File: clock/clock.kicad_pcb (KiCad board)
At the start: 2 copper layers, 176.8 x 81.3 mm, 288 parts, among them P101 CONN_01X03, P102 CONN_FAN_PWM, P103 XG4A-1631, P301 MCRF, Q201 MMBT3904, U201 PCA9306, U202 DAC8830, U203 LMV722, U204 LTC2990, U205 LP3853, U207 NC7SZ125, U301 Adafruit746, U302 MIC5225, U303 PA6H, U401 74LVC541, U501 TPS56428, U502 TPS56428, U503 TPS56428, U601 ADT7410, U602 DS3231, U603 ADT7410, Y202 CX210

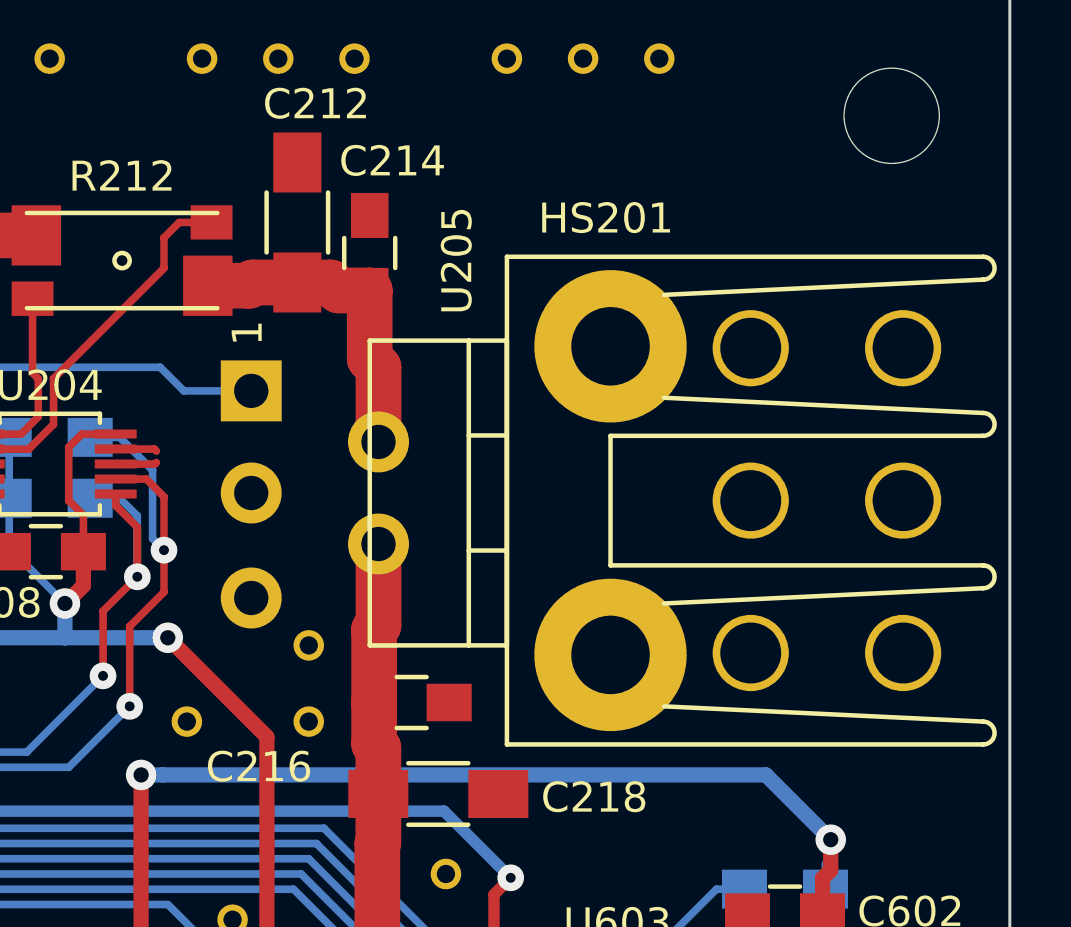
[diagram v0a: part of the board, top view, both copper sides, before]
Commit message: Fix pin location on to-220 and heatsink location. Add 7-segment display 3D model to board.
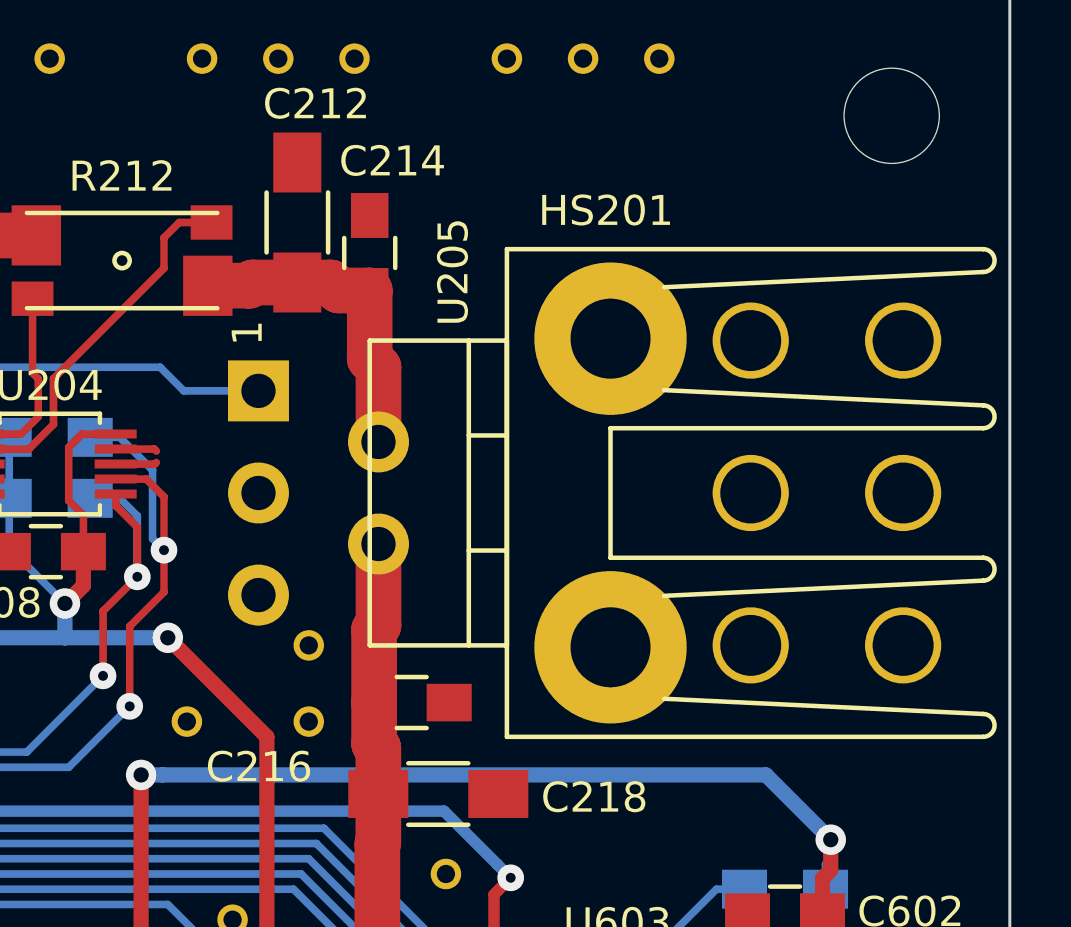
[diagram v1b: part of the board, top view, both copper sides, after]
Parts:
- moved HS201 0.25 mm to (350.5, 181.6)
- moved REF** 0.25 mm to (358.6, 186.7)
- moved REF** 0.25 mm to (363.7, 186.7)
- moved REF** 0.25 mm to (363.7, 176.5)
- moved REF** 0.25 mm to (363.7, 181.6)
- moved REF** 0.25 mm to (358.6, 176.5)
- moved REF** 0.25 mm to (358.6, 181.6)

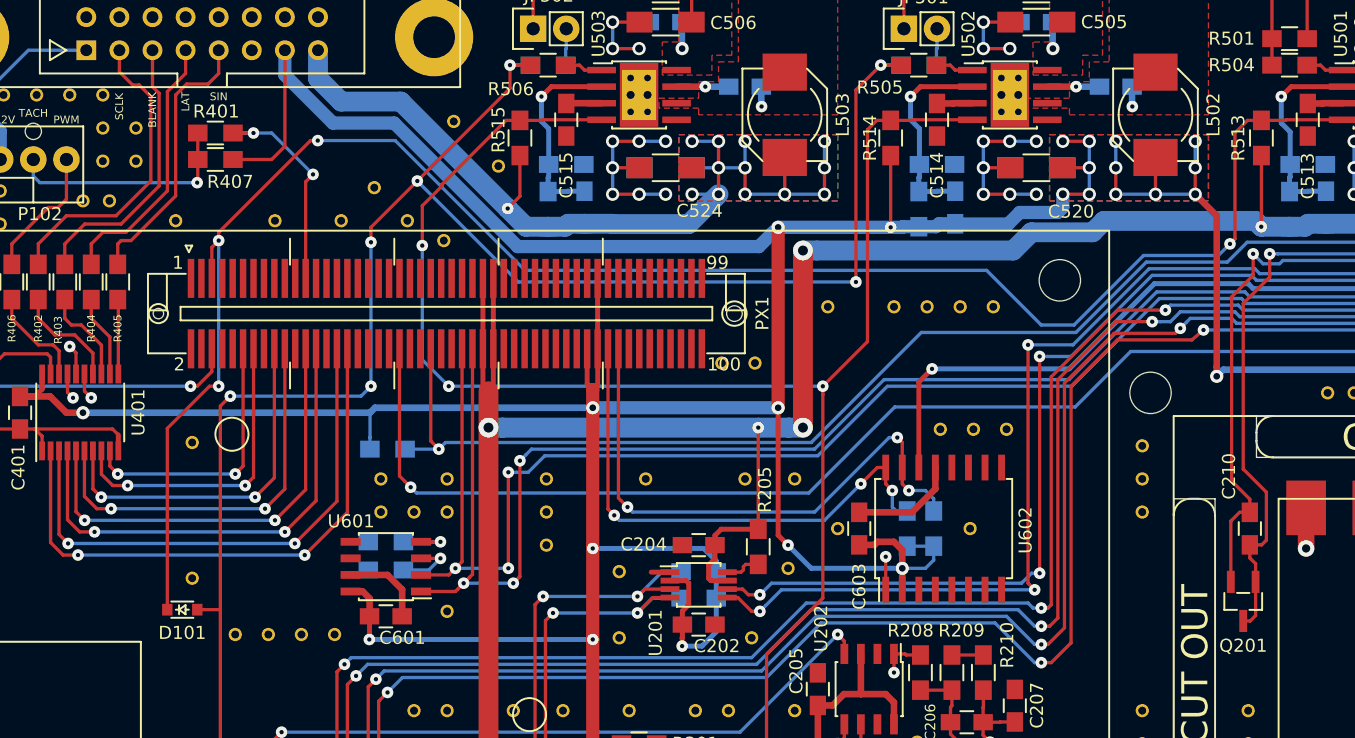
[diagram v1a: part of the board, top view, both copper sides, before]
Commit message: Add inductor and sot-23 3d models.
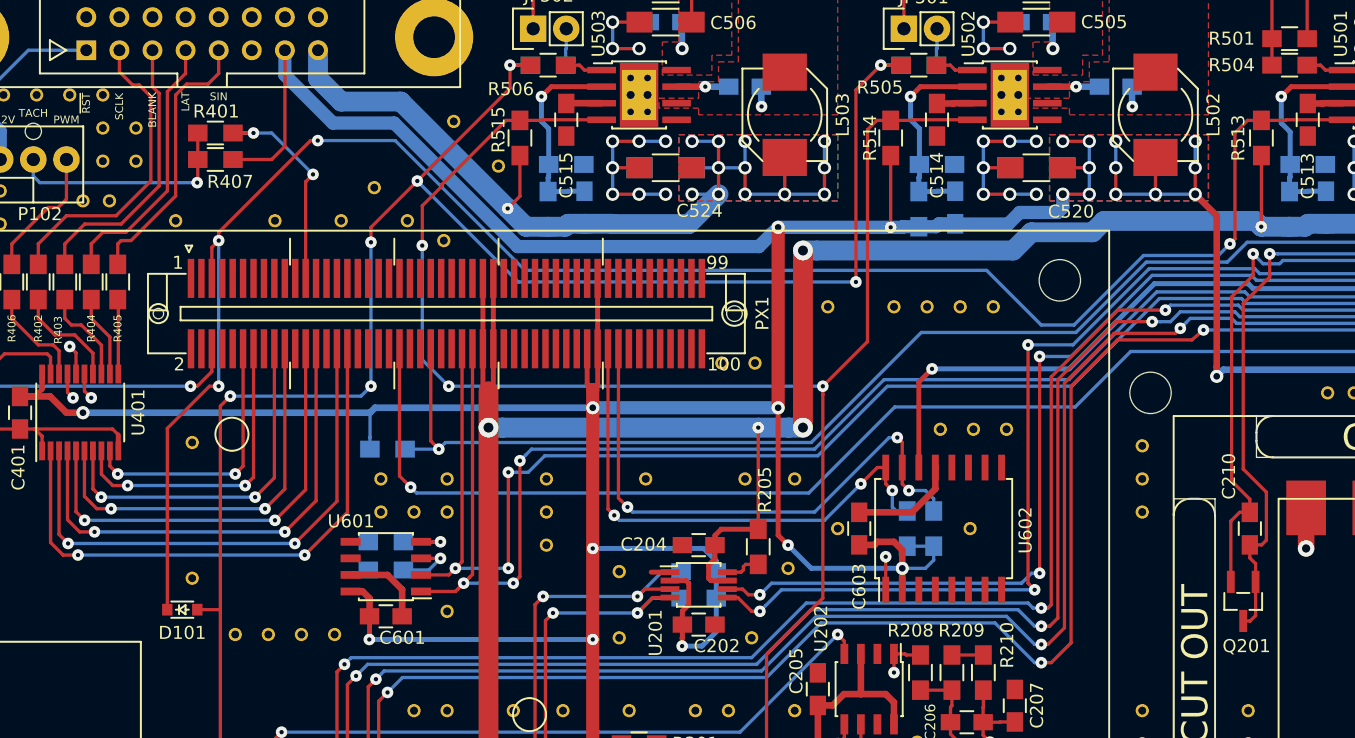
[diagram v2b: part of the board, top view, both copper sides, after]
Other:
- board text added: "~RST~"
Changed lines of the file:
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@@
     (area 190.449999 165.049999 367.334001 246.430001)
     (thickness 1.6)
-    (drawings 69)
+    (drawings 70)
     (tracks 1497)
     (zones 0)
@@
     (pad 2 smd rect (at 3.275 0 270) (size 2.85 3.4) (layers F.Cu F.Paste F.Mask)
       (net 4 VIN) (zone_connect 2))
+    (model /home/guest/cae/kicad/mod/local.pretty/packages3d/spm6530.wrl
+      (at (xyz 0 0 0))
+      (scale (xyz 0.393700787402 0.393700787402 0.393700787402))
+      (rotate (xyz 0 0 0))
+    )
   )
   (module local:Choke_SMD_7.1x6.5_H3.0_HandSoldering (layer F.Cu)
@@
     (pad 2 smd rect (at 3.275 0 270) (size 2.85 3.4) (layers F.Cu F.Paste F.Mask)
       (net 3 VCC) (zone_connect 2))
+    (model /home/guest/cae/kicad/mod/local.pretty/packages3d/spm6530.wrl
+      (at (xyz 0 0 0))
+      (scale (xyz 0.393701 0.393700787402 0.393700787402))
+      (rotate (xyz 0 0 0))
+    )
   )
   (module local:Choke_SMD_7.1x6.5_H3.0_HandSoldering (layer F.Cu)
@@
     (pad 2 smd rect (at 3.275 0 270) (size 2.85 3.4) (layers F.Cu F.Paste F.Mask)
       (net 16 /power/+3.0V) (zone_connect 2))
+    (model /home/guest/cae/kicad/mod/local.pretty/packages3d/spm6530.wrl
+      (at (xyz 0 0 0))
+      (scale (xyz 0.393700787402 0.393700787402 0.393700787402))
+      (rotate (xyz 0 0 0))
+    )
   )
   (module local:Terminal_Block_1x03 (layer F.Cu)
@@
     (tags SOT-23)
     (attr smd)
-    (fp_text reference Q201 (at 0 -3.4 180) (layer F.SilkS)
+    (fp_text reference Q201 (at -0.254 -3.429 180) (layer F.SilkS)
       (effects (font (size 1 1) (thickness 0.15)))
     )
@@
     (pad 3 smd rect (at 0 -1.5 180) (size 0.6 1.7) (layers F.Cu F.Paste F.Mask)
       (net 110 /ocxo/TSENSE_A))
-    (model Housings_SOT-23_SOT-143_TSOT-6.3dshapes/SOT-23.wrl
+    (model TO_SOT_Packages_SMD.3dshapes/SOT-23.wrl
       (at (xyz 0 0 0))
       (scale (xyz 1 1 1))
@@
     )
   )
+  (gr_text ~RST~ (at 213.614 179.451 90) (layer F.SilkS)
+    (effects (font (size 0.6 0.6) (thickness 0.127)))
+  )
   (gr_text PWM (at 212.09 180.721) (layer F.SilkS)

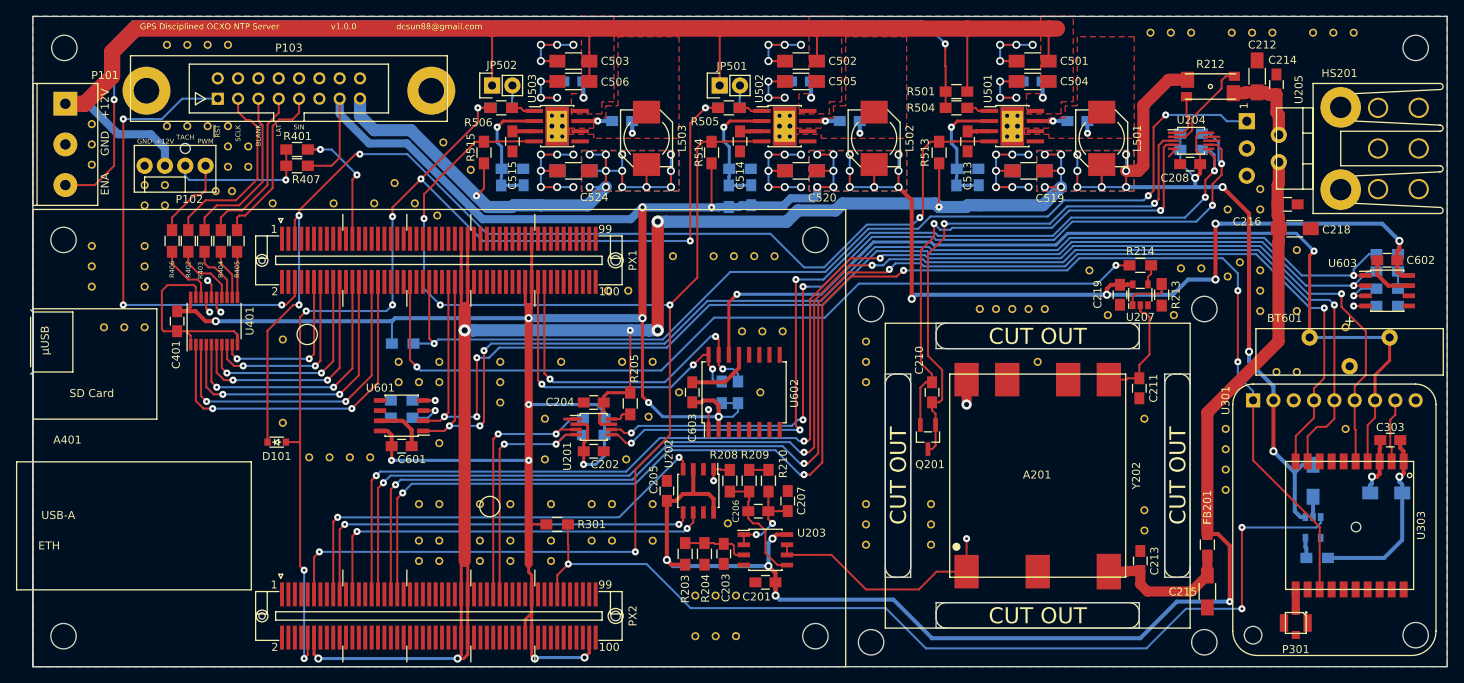
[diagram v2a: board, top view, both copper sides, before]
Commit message: Checkpoint pin swaps and addition of 3D models.
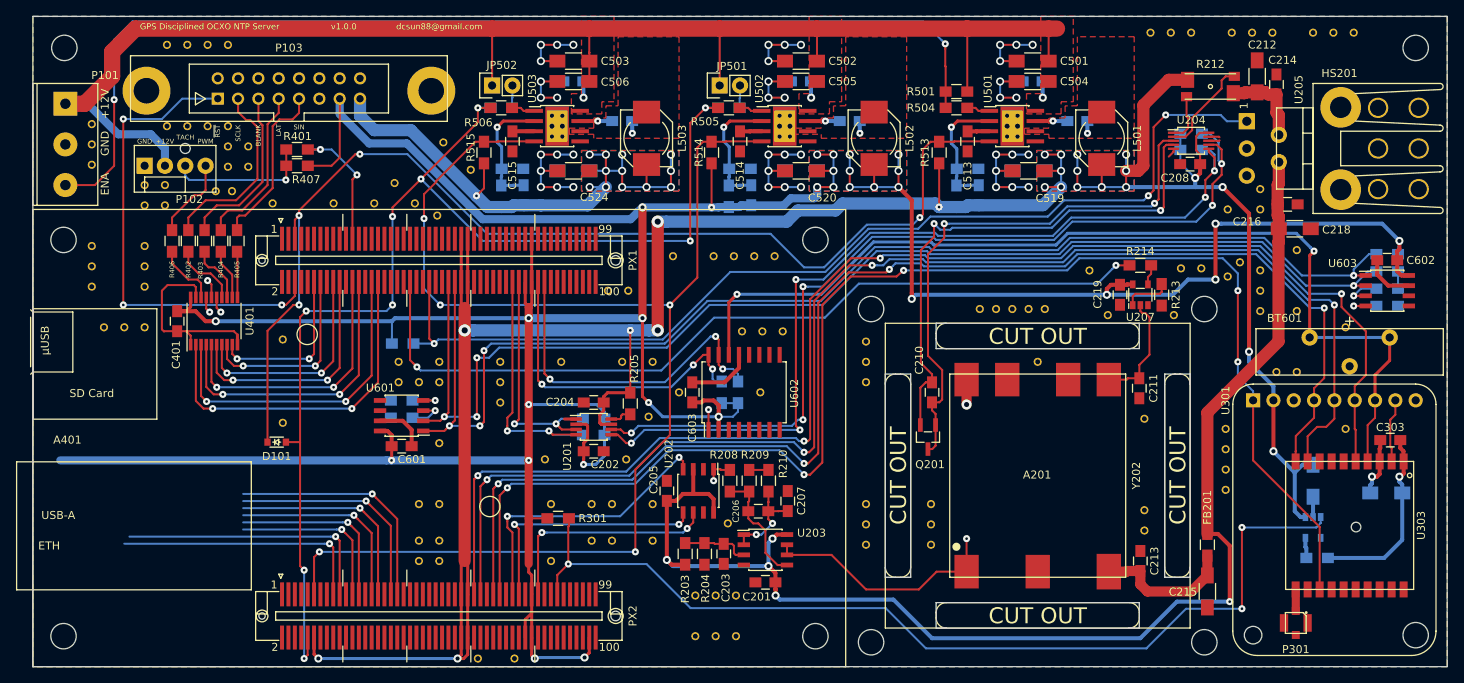
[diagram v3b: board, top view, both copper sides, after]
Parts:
- removed the REF** at (254.5, 215.4)
- removed the REF** at (232.7, 220.2)
- removed the REF** at (230.1, 220.2)
- removed the REF** at (227.6, 220.2)
- removed the REF** at (225.0, 220.2)
- removed the REF** at (255.3, 230.6)
- removed the REF** at (250.2, 233.2)
- removed the REF** at (246.4, 233.2)
- removed the REF** at (246.4, 230.6)
- removed the REF** at (250.2, 230.6)
- removed the REF** at (250.2, 226.1)
- removed the REF** at (246.4, 226.1)
- added REF**: Stitching_Via_40x24mil, local:Stitching_Via_40x24mil, F.Cu at (250.7, 245.4)
- added REF**: Stitching_Via_40x24mil, local:Stitching_Via_40x24mil, F.Cu at (246.1, 245.4)
- moved R301 0.77 mm to (256.2, 227.8)
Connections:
- PX1 pad 74: /microzed/PX1_LVDS_21_P -> /microzed/OCXO_SDA
- PX1 pad 76: /microzed/PX1_LVDS_21_N -> /microzed/OCXO_SCL
- PX2 pad 17: /microzed/~DAC_CS~ -> /microzed/PX2_LVDS_0_P
- PX2 pad 19: /microzed/DAC_SCLK -> /microzed/PX2_LVDS_0_N
- PX2 pad 23: /ocxo/DAC_SDI -> /microzed/PX2_LVDS_2_P
- PX2 pad 29: /gps/3DFIX -> /microzed/PX2_LVDS_4_P
- PX2 pad 31: /microzed/GPS_TX -> /microzed/PX2_LVDS_4_N
- PX2 pad 35: /microzed/GPS_RX -> /microzed/PX2_LVDS_6_P
- PX2 pad 37: /gps/1PPS -> /microzed/PX2_LVDS_6_N
- PX2 pad 61: /microzed/PX2_LVDS_14_P -> /gps/3DFIX
- PX2 pad 63: /microzed/PX2_LVDS_14_N -> /microzed/GPS_TX
- PX2 pad 67: /microzed/OCXO_SCL -> /microzed/GPS_RX
- PX2 pad 69: /microzed/OCXO_SDA -> /gps/1PPS
- PX2 pad 73: /microzed/PX2_LVDS_18_P -> /microzed/~DAC_CS~
- PX2 pad 75: /microzed/PX2_LVDS_18_N -> /microzed/DAC_SCLK
- PX2 pad 81: /microzed/PX2_LVDS_20_P -> /ocxo/DAC_SDI
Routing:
- net VCC: track 443.3 -> 484.8 mm
- net /microzed/PX2_LVDS_0_N: track 0.00 -> 33.2 mm, vias 0 -> 1
- net /microzed/PX2_LVDS_0_P: track 0.00 -> 32.2 mm, vias 0 -> 1
- net /microzed/PX2_LVDS_6_N: track 0.00 -> 30.0 mm, vias 0 -> 1
- net /microzed/PX2_LVDS_6_P: track 0.00 -> 28.3 mm, vias 0 -> 1
- net /microzed/PX2_LVDS_4_N: track 0.00 -> 26.3 mm, vias 0 -> 1
- net /microzed/PX2_LVDS_4_P: track 0.00 -> 24.6 mm, vias 0 -> 1
- net /ocxo/DAC_SDI: track 51.8 -> 29.0 mm
- net /microzed/PX2_LVDS_2_N: track 0.00 -> 22.6 mm, vias 0 -> 1
- net /microzed/DAC_SCLK: track 52.5 -> 31.3 mm
- net /microzed/~DAC_CS~: track 57.3 -> 36.2 mm
- net /microzed/PX2_LVDS_2_P: track 0.00 -> 21.0 mm, vias 0 -> 1
- net /microzed/GPS_RX: track 178.5 -> 165.8 mm
- net /gps/3DFIX: track 183.8 -> 171.1 mm
- net /microzed/GPS_TX: track 181.7 -> 169.0 mm
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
